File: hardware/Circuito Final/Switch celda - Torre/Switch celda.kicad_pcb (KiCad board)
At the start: 2 copper layers, 98.6 x 38 mm, 28 parts, among them Q1 MMBT2222A, Q2 MMBT2907A, Q3 MMBT2222A

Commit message: update pcb celdas
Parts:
- added H1: MountingHole, MountingHole:MountingHole_3.5mm, F.Cu at (61.5, 55.0)
- added H2: MountingHole, MountingHole:MountingHole_3.5mm, F.Cu at (74.0, 55.0)
- added H3: MountingHole, MountingHole:MountingHole_3.5mm, F.Cu at (61.5, 68.5)
- added H4: MountingHole, MountingHole:MountingHole_3.5mm, F.Cu at (74.0, 68.0)
- added J_In_cell_neg_1: Conn_01x07_Socket, Connector_PinSocket_2.54mm:PinSocket_1x07_P2.54mm_Vertical, F.Cu at (123.5, 53.9)
- added Jumper_Vcell_1: Conn_01x07_Pin, Connector_PinHeader_2.54mm:PinHeader_1x07_P2.54mm_Vertical, F.Cu at (93.9, 53.9)
- added Jumper_cell_neg_1: Conn_01x07_Pin, Connector_PinHeader_2.54mm:PinHeader_1x07_P2.54mm_Vertical, F.Cu at (108.5, 53.9)

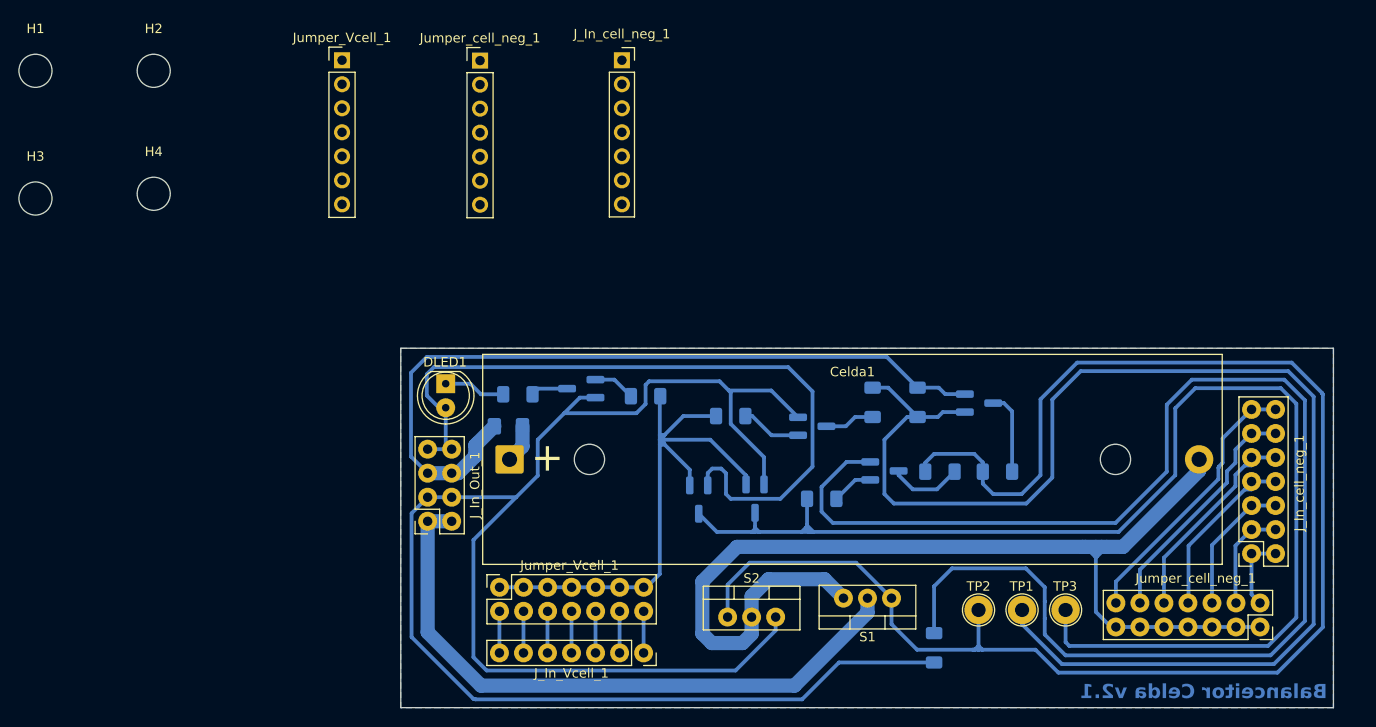
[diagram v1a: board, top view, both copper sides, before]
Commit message: PCB celda con los orificios para las varillas colocados y reduciendo la cantidad de pines hembra macho a la mitad
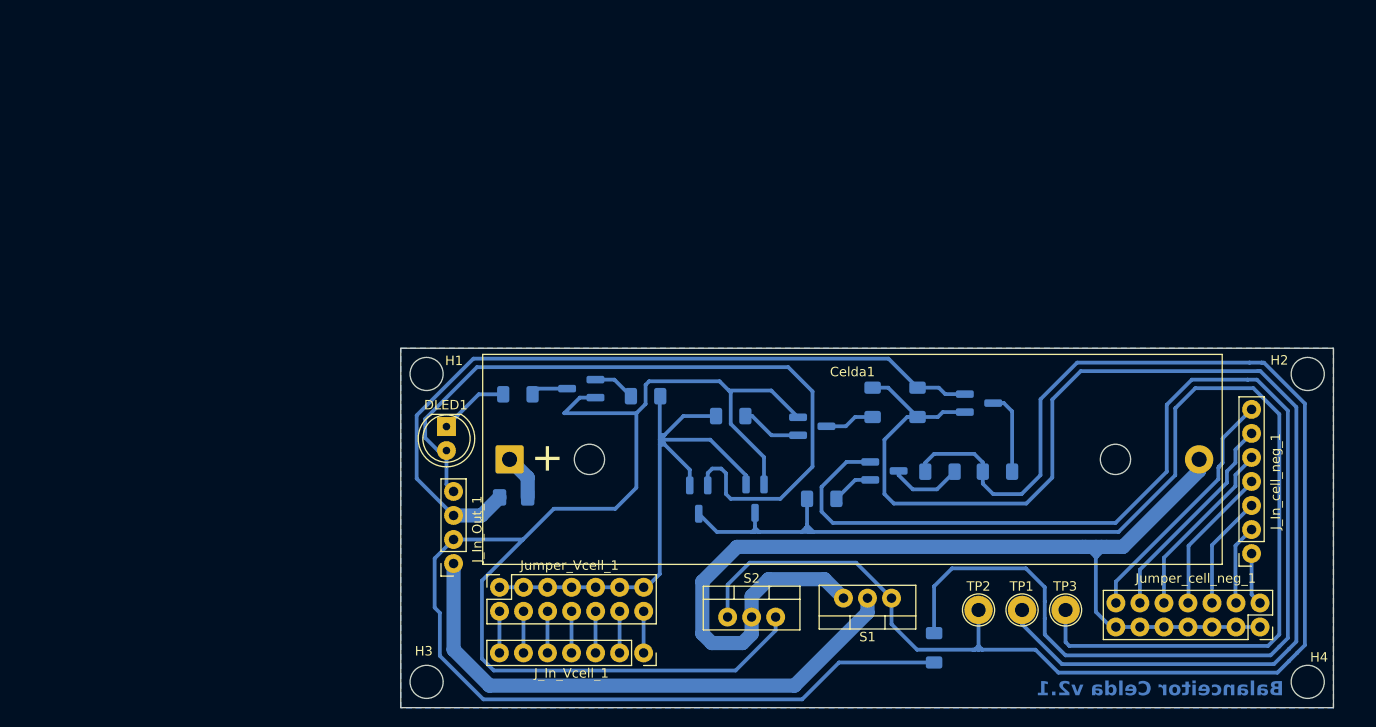
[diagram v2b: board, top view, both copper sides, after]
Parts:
- removed the J_In_cell_neg_1 at (190.1, 106.0)
- removed the Jumper_Vcell_1 at (93.9, 53.9)
- removed the Jumper_cell_neg_1 at (108.5, 53.9)
- J_In_Out_1: value Conn_02x04_Odd_Even -> Conn_01x04_Socket; footprint Connector_PinSocket_2.54mm:PinSocket_2x04_P2.54mm_Vertical -> Connector_PinSocket_2.54mm:PinSocket_1x04_P2.54mm_Vertical
- moved H4 132.5 mm to (196.0, 119.6)
- moved H2 126.1 mm to (196.0, 87.0)
- moved J_In_cell_neg_1 84.6 mm to (190.1, 106.0), turned to 180 degrees
- moved H3 65.7 mm to (102.8, 119.6)
- moved H1 52.3 mm to (102.8, 87.0)
- moved F1 7.54 mm to (112.0, 100.1)
- moved J_In_Out_1 5.24 mm to (105.7, 107.1)
- moved DLED1 4.53 mm to (105.0, 92.6)
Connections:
- J_In_Out_1 pad 2: bus_neg -> 0
- J_In_Out_1 pad 3: 0 -> bus_pos
- J_In_Out_1 pad 4: 0 -> Vcc
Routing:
- net bus_neg: track 67.8 -> 59.2 mm
- net 0: track 342.5 -> 337.2 mm
- net Net-(S1-G): track 164.2 -> 160.9 mm
- net Net-(Q2-B): track 138.9 -> 135.7 mm
- net Net-(Qinv1-D): track 136.5 -> 133.3 mm
- net cell_neg5: track 22.2 -> 19.2 mm
- net cell_neg4: track 18.6 -> 15.6 mm
- net cell_neg6: track 25.3 -> 22.8 mm
- net cell_neg2: track 11.0 -> 8.49 mm
- net cell_neg7: track 28.9 -> 26.4 mm
- net cell_neg3: track 14.6 -> 12.0 mm
- net cell_neg1: track 8.13 -> 5.59 mm
- net bus_pos: track 82.4 -> 80.3 mm
- net Net-(DLED1-K): track 6.54 -> 7.41 mm
- net Net-(Celda1-+): track 4.07 -> 4.81 mm

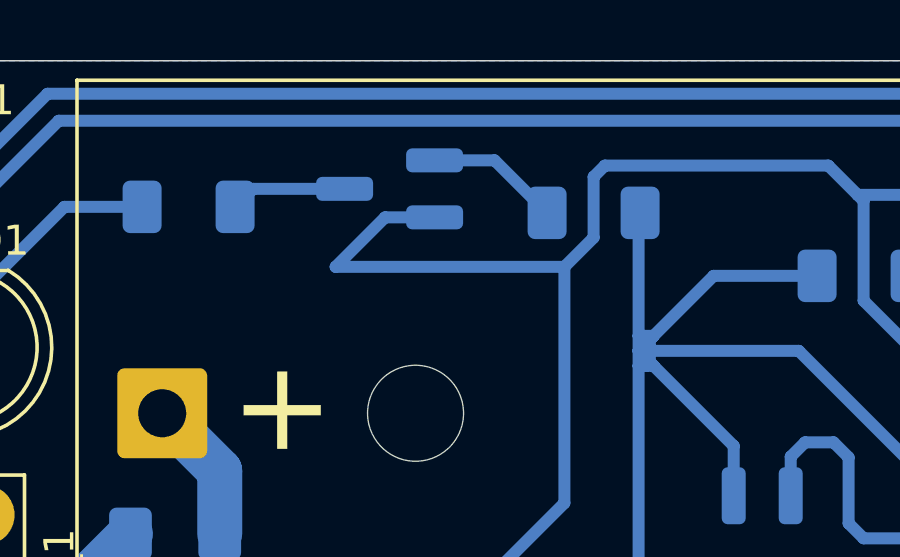
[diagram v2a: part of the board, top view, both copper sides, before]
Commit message: update menor del pcb de las celdas
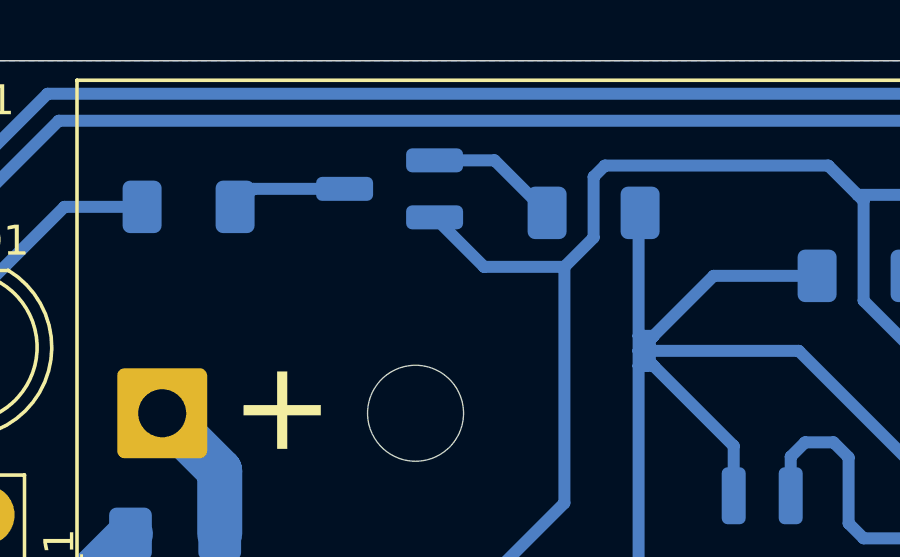
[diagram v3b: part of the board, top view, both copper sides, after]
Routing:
- net 0: track 337.2 -> 330.6 mm
